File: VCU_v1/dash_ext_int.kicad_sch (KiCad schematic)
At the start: 33 parts, among them U15 SP8K80TB1, U16 SP8K80TB1

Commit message: left to do before layout: wire DRS/Debug LEDs to connector, add BRUHbus ports
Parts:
- removed D23, D3, D4: MM3Z3V3T1G, Diode_SMD:D_SOD-323_HandSoldering, symbol .Diode-Zener:MM3Z3V3T1G
- removed R31, R33, R35: 6.2k, Resistor_SMD:R_0603_1608Metric_Pad0.98x0.95mm_HandSolder, symbol BFR Resistors:RMCF0603FT6K20
- removed R32, R34, R36: 1.0k, Resistor_SMD:R_0603_1608Metric_Pad0.98x0.95mm_HandSolder, symbol BFR Resistors:RMCF0603FT1K00
- added R31, R33, R35: 100, Resistor_SMD:R_0603_1608Metric_Pad0.98x0.95mm_HandSolder, symbol BFR Resistors:RMCF0603FT100R
- added R32, R34, R36, R54, R55, R56: 10k, Resistor_SMD:R_0603_1608Metric_Pad0.98x0.95mm_HandSolder, symbol BFR Resistors:RMCF0603FT10K0
- added U18, U19: SP8K80TB1, symbol SP8KK80TB1:SP8K80TB1
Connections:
- net BMS-3.3: now also R55.1, U18.5 (DRAIN2), U18.6 (DRAIN2)
- net BMS-FAULT: now also R33.1
- net BSPD-3.3: now also R54.1, U18.7 (DRAIN1), U18.8 (DRAIN1)
- net BSPD-FAULT: now also R31.1
- net GND: now also R32.1, R34.1, R36.1, U18.1 (SOURCE1), U18.3 (SOURCE2), U19.1 (SOURCE1)
- net IMD-3.3: now also R56.1, U19.7 (DRAIN1), U19.8 (DRAIN1)
- net IMD-FAULT: now also R35.1
- new net: R33.2, R34.2, U18.4 (GATE2)
- new net: R31.2, R32.2, U18.2 (GATE1)
- new net: R35.2, R36.2, U19.2 (GATE1)
- new net +3.3V: R54.2, R55.2, R56.2
- no-connect marks 4 -> 8

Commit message: v1 schematic (actually) complete, let the layout commence
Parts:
- removed R39, R40, R41: 1.2k, Resistor_SMD:R_0603_1608Metric_Pad0.98x0.95mm_HandSolder, symbol BFR Resistors:RMCF0603FT1K20
- removed U15, U16, U18, U19: SP8K80TB1, symbol SP8KK80TB1:SP8K80TB1
- added Q3, Q4, Q5: SP8K80TB1, Package_SO:SOP-8_3.76x4.96mm_P1.27mm, symbol Transistor_FET:Q_Dual_NMOS_S1G1S2G2D2D2D1D1
- added R54, R60, R69: 10k, Resistor_SMD:R_0603_1608Metric_Pad0.98x0.95mm_HandSolder, symbol BFR Resistors:RMCF0603FT10K0
- added R55, R62, R70: 100, Resistor_SMD:R_0603_1608Metric_Pad0.98x0.95mm_HandSolder, symbol BFR Resistors:RMCF0603FT100R
- added R57, R65, R71: 1.6k, Resistor_SMD:R_0603_1608Metric_Pad0.98x0.95mm_HandSolder, symbol BFR Resistors:RMCF0603FT1K60
- added TP27, TP28, TP29, TP30, TP31, TP32, TP33, TP34, TP35, TP36, TP37, TP38, TP39, TP40, TP41: RH-5015, TestPoint:TestPoint_Keystone_5015_Micro_Mini, symbol .Test-Point:RH-5015
- renumbered C119 to C81, C50 to C82, C49 to C83, C51 to C84, D5 to D8, R32 to R43, R34 to R44, R31 to R45, R33 to R46, R37 to R47, R38 to R48, R36 to R49, R35 to R50, R54 to R51, R55 to R52, R56 to R53, R109 to R56, R62 to R58, R119 to R59, R45 to R61, R46 to R63, R47 to R64, R42 to R66, R43 to R67, R44 to R68, R48 to R72, R49 to R73, R50 to R74
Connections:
- net +24V: now also R57.2, R65.2, R71.2
- net BMS-3.3: now also Q3.5 (D), Q3.6 (D), TP29.1
- net BMS-FAULT: now also R44.2, R60.2, R62.1, TP30.1
- net BMS_LED+: now also Q5.7 (D), Q5.8 (D), R65.1, TP40.1
- net BMS_LED-: now also Q5.1 (S), R60.1
- net BRAKE-LIGHT: now also TP33.1
- net BRAKE-LIGHT-3.3: now also TP34.1
- net BSPD-3.3: now also Q3.7 (D), Q3.8 (D), TP27.1
- net BSPD-FAULT: now also R43.2, R54.2, R55.1, TP28.1
- net BSPD_LED+: now also Q4.5 (D), Q4.6 (D), R57.1, TP39.1
- net BUTTON-1-SIG: now also TP35.1
- net BUTTON-2-SIG: now also TP36.1
- net BUTTON-3-SIG: now also TP37.1
- net BUTTON-4-SIG: now also TP38.1
- net GND: now also Q3.1 (S), Q3.3 (S), Q4.1 (S), Q4.3 (S), R54.1
- net IMD-3.3: now also Q4.7 (D), Q4.8 (D), TP31.1
- net IMD-FAULT: now also R49.2, R69.2, R70.1, TP32.1
- net IMD_LED+: now also Q5.5 (D), Q5.6 (D), R71.1, TP41.1
- net IMD_LED-: now also Q5.3 (S), R69.1
- net at R46.2: now also Q3.4 (G); no longer R44.2
- net at R45.2: now also Q3.2 (G); no longer R43.2
- net at R50.2: now also Q4.2 (G); no longer R49.2
- new net: Q5.4 (G), R70.2
- new net: Q4.4 (G), R55.2
- new net: Q5.2 (G), R62.2
- no-connect marks 8 -> 0
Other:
- moved on the sheet: R43, R45, R46, R50

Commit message: begin pcb design
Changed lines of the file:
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@@
 	)
 	(junction
-		(at 64.6693 87.63)
-		(diameter 0)
-		(color 0 0 0 0)
-	)
-	(junction
 		(at 125.73 102.87)
 		(diameter 0)
@@
 	)
 	(junction
+		(at 64.77 87.63)
+		(diameter 0)
+		(color 0 0 0 0)
+	)
+	(junction
 		(at 67.31 124.46)
 		(diameter 0)
@@
 	(wire
 		(pts
-			(xy 58.42 87.63) (xy 64.6693 87.63)
+			(xy 58.42 87.63) (xy 64.77 87.63)
 		)
 		(stroke
@@
 	(wire
 		(pts
+			(xy 64.77 87.63) (xy 68.58 87.63)
+		)
+		(stroke
+			(width 0)
+			(type default)
+		)
+	)
+	(wire
+		(pts
 			(xy 168.91 69.85) (xy 168.91 73.66)
 		)
@@
 	(wire
 		(pts
-			(xy 64.6693 87.63) (xy 68.58 87.63)
-		)
-		(stroke
-			(width 0)
-			(type default)
-		)
-	)
-	(wire
-		(pts
 			(xy 163.83 130.81) (xy 163.83 138.43)
 		)
@@
 	(symbol
 		(lib_id ".Test-Point:RH-5015")
-		(at 64.6693 87.63 0)
+		(at 64.77 87.63 0)
 		(unit 1)
 		(exclude_from_sim no)
@@
 		(dnp no)
 		(property "Reference" "TP29"
-			(at 63.1461 82.3737 0)
+			(at 63.2468 82.3737 0)
 			(effects
 				(font
@@
 		)
 		(property "Value" "RH-5015"
-			(at 63.1461 80.2235 0)
+			(at 63.2468 80.2235 0)
 			(effects
 				(font
@@
 		)
 		(property "Footprint" "TestPoint:TestPoint_Keystone_5015_Micro_Mini"
-			(at 64.6693 99.06 0)
+			(at 64.77 99.06 0)
 			(effects
 				(font
@@
 		)
 		(property "Datasheet" "https://wmsc.lcsc.com/wmsc/upload/file/pdf/v2/lcsc/2310260935_ronghe-RH-5015_C5199798.pdf"
-			(at 64.6693 102.87 0)
+			(at 64.77 102.87 0)
 			(effects
 				(font
@@
 		)
 		(property "Description" "Surface-mount grabby test point"
-			(at 64.6693 106.68 0)
+			(at 64.77 106.68 0)
 			(effects
 				(font
@@
 		)
 		(property "Link" "https://jlcpcb.com/partdetail/Ronghe-RH5015/C5199798"
-			(at 64.6693 110.49 0)
+			(at 64.77 110.49 0)
 			(effects
 				(font
@@
 		)
 		(property "Digikey P/N" "36-5015CT-ND"
-			(at 64.6693 121.92 0)
+			(at 64.77 121.92 0)
 			(effects
 				(font
@@
 		)
 		(property "Mouser P/N" "534-5015"
-			(at 64.6693 125.73 0)
+			(at 64.77 125.73 0)
 			(effects
 				(font
@@
 		)
 		(property "LCSC P/N" "C5199798"
-			(at 64.6693 129.54 0)
+			(at 64.77 129.54 0)
 			(effects
 				(font
@@
 		)
 		(property "Manufacturer" "Ronghe"
-			(at 64.6693 114.3 0)
+			(at 64.77 114.3 0)
 			(effects
 				(font
@@
 		)
 		(property "Manufacturer P/N" "RH-5015"
-			(at 64.6693 118.11 0)
+			(at 64.77 118.11 0)
 			(effects
 				(font
@@
 		)
 		(property "LCSC Part #" "C5199798"
-			(at 64.6693 87.63 0)
+			(at 64.77 87.63 0)
 			(effects
 				(font

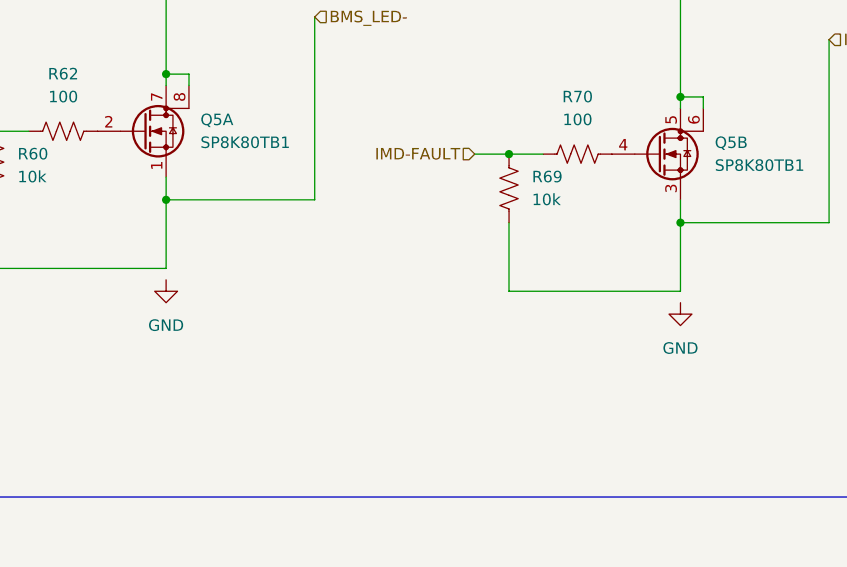
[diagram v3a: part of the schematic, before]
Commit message: vcu placements complete
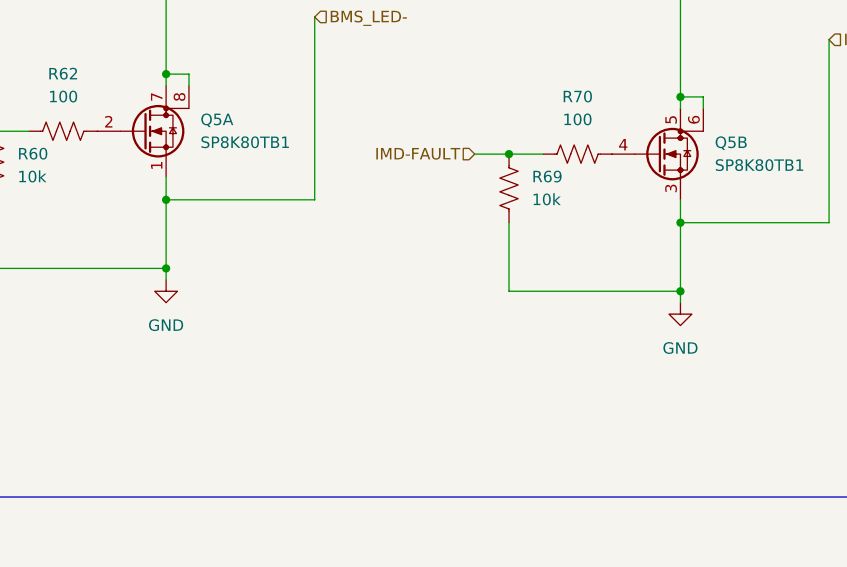
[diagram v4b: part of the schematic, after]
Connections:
- net BMS_LED- is gone; now on net GND: Q5.1 (S), R60.1
- net IMD_LED- is gone; now on net GND: Q5.3 (S), R69.1

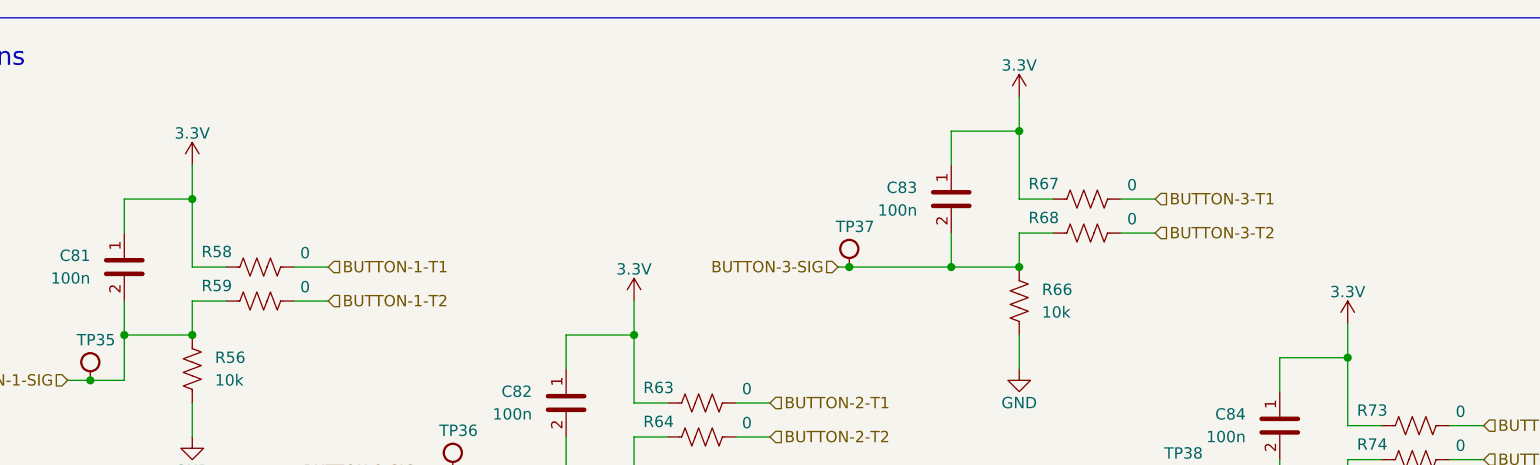
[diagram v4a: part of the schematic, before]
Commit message: stm power routing complete, power polygons done
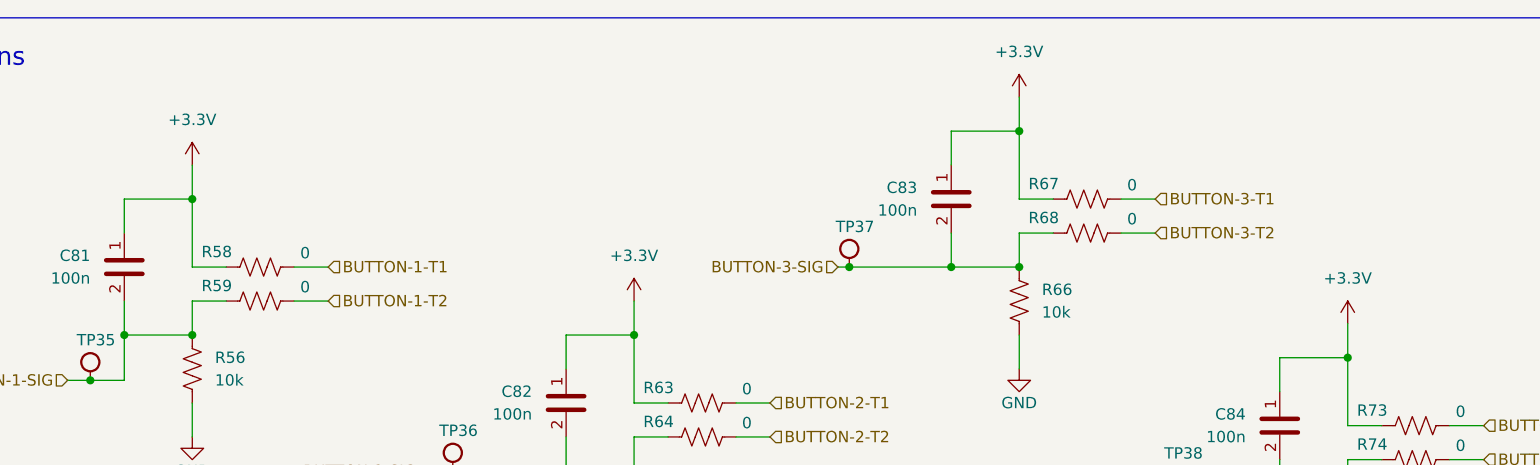
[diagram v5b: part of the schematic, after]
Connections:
- net 3.3V is gone; now on net +3.3V: C81.1, C82.1, C83.1, C84.1, R58.1, R63.1, R67.1, R73.1

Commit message: almost done i promise
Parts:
- removed R57, R65, R71: 1.6k, Resistor_SMD:R_0603_1608Metric_Pad0.98x0.95mm_HandSolder, symbol BFR Resistors:RMCF0603FT1K60
- added R4, R7, R8: 2.4k, Resistor_SMD:R_0603_1608Metric_Pad0.98x0.95mm_HandSolder, symbol BFR Resistors:RMCF0603FT2K40
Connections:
- net BMS_LED+: now also R7.1
- net BSPD_LED+: now also R4.1
- net IMD_LED+: now also R8.2
- new net +12V: R4.2, R7.2, R8.1
